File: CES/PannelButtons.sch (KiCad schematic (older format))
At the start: 16 parts

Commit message: Control Unit
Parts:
- gave numbers to parts that had none: 12
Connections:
- net BotEscM renamed BotMem
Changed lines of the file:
@@
 $Descr A4 11693 8268
 encoding utf-8
-Sheet 14 16
+Sheet 15 17
 Title ""
 Date ""
@@
 $EndDescr
 $Comp
-L Connector:Conn_01x08_Male J?
+L Connector:Conn_01x08_Male J1501
 U 1 1 61251A95
 P 700 6900
-F 0 "J?" H 800 6400 50  0000 C CNN
+F 0 "J1501" H 800 6400 50  0000 C CNN
 F 1 "PannelButtonsConnector" H 1200 7450 50  0000 C CNN
 F 2 "" H 700 6900 50  0001 C CNN
@@
 ~_IntPara
 $Comp
-L power:VCC #PWR?
+L power:VCC #PWR01501
 U 1 1 6085AA0D
 P 1450 900
-F 0 "#PWR?" H 1450 750 50  0001 C CNN
+F 0 "#PWR01501" H 1450 750 50  0001 C CNN
 F 1 "VCC" H 1465 1073 50  0000 C CNN
 F 2 "" H 1450 900 50  0001 C CNN
@@
 $EndComp
 $Comp
-L Device:R R?
+L Device:R R1501
 U 1 1 6085B8ED
 P 1450 1150
-F 0 "R?" H 1520 1196 50  0000 L CNN
+F 0 "R1501" H 1520 1196 50  0000 L CNN
 F 1 "1k5" H 1520 1105 50  0000 L CNN
 F 2 "" V 1380 1150 50  0001 C CNN
@@
 Connection ~ 1450 1450
 $Comp
-L 74xx:74HC00 U?
+L 74xx:74HC00 U1501
 U 1 1 6085C645
 P 7700 1050
-F 0 "U?" H 7700 1375 50  0000 C CNN
+F 0 "U1501" H 7700 1375 50  0000 C CNN
 F 1 "74HC00" H 7700 1284 50  0000 C CNN
 F 2 "" H 7700 1050 50  0001 C CNN
@@
 $EndComp
 $Comp
-L 74xx:74HC00 U?
+L 74xx:74HC00 U1501
 U 2 1 6085FDDA
 P 7700 1750
-F 0 "U?" H 7700 2075 50  0000 C CNN
+F 0 "U1501" H 7700 2075 50  0000 C CNN
 F 1 "74HC00" H 7700 1984 50  0000 C CNN
 F 2 "" H 7700 1750 50  0001 C CNN
@@
 $EndComp
 $Comp
-L 74xx:74HC00 U?
+L 74xx:74HC00 U1501
 U 3 1 60862050
 P 4250 1000
-F 0 "U?" H 4250 1325 50  0000 C CNN
+F 0 "U1501" H 4250 1325 50  0000 C CNN
 F 1 "74HC00" H 4250 1234 50  0000 C CNN
 F 2 "" H 4250 1000 50  0001 C CNN
@@
 $EndComp
 $Comp
-L 74xx:74HC00 U?
+L 74xx:74HC00 U1501
 U 4 1 60863680
 P 4250 1600
-F 0 "U?" H 4250 1925 50  0000 C CNN
+F 0 "U1501" H 4250 1925 50  0000 C CNN
 F 1 "74HC00" H 4250 1834 50  0000 C CNN
 F 2 "" H 4250 1600 50  0001 C CNN
@@
 $EndComp
 $Comp
-L 74xx:74HC00 U?
+L 74xx:74HC00 U1501
 U 5 1 608648EA
 P 3900 6750
-F 0 "U?" H 4130 6796 50  0000 L CNN
+F 0 "U1501" H 4130 6796 50  0000 L CNN
 F 1 "74HC00" H 4130 6705 50  0000 L CNN
 F 2 "" H 3900 6750 50  0001 C CNN
@@
 	5650 950  6750 950
 $Comp
-L Device:R R?
+L Device:R R1508
 U 1 1 6086CFA4
 P 6750 1450
-F 0 "R?" H 6820 1496 50  0000 L CNN
+F 0 "R1508" H 6820 1496 50  0000 L CNN
 F 1 "1k5" H 6820 1405 50  0000 L CNN
 F 2 "" V 6680 1450 50  0001 C CNN
@@
 $EndComp
 $Comp
-L Device:R R?
+L Device:R R1507
 U 1 1 6086D527
 P 6750 750
-F 0 "R?" H 6820 796 50  0000 L CNN
+F 0 "R1507" H 6820 796 50  0000 L CNN
 F 1 "1k5" H 6820 705 50  0000 L CNN
 F 2 "" V 6680 750 50  0001 C CNN
@@
 $EndComp
 $Comp
-L power:VCC #PWR?
+L power:VCC #PWR01511
 U 1 1 6086DE5E
 P 6750 500
-F 0 "#PWR?" H 6750 350 50  0001 C CNN
+F 0 "#PWR01511" H 6750 350 50  0001 C CNN
 F 1 "VCC" H 6765 673 50  0000 C CNN
 F 2 "" H 6750 500 50  0001 C CNN
@@
 $EndComp
 $Comp
-L power:VCC #PWR?
+L power:VCC #PWR01512
 U 1 1 6086E407
 P 6750 1200
-F 0 "#PWR?" H 6750 1050 50  0001 C CNN
+F 0 "#PWR01512" H 6750 1050 50  0001 C CNN
 F 1 "VCC" H 6765 1373 50  0000 C CNN
 F 2 "" H 6750 1200 50  0001 C CNN
@@
 P 9450 2050
 AR Path="/611BF25E/6087FD7D" Ref="U?"  Part="6"
-AR Path="/60832DB9/6125152F/6087FD7D" Ref="U?"  Part="6"
-F 0 "U?" H 9450 2367 50  0000 C CNN
+AR Path="/60832DB9/6125152F/6087FD7D" Ref="U1502"  Part="6"
+F 0 "U1502" H 9450 2367 50  0000 C CNN
 F 1 "74HC14" H 9450 2276 50  0000 C CNN
 F 2 "" H 9450 2050 50  0001 C CNN
@@
 _BotMudaP
 $Comp
-L power:VCC #PWR?
+L power:VCC #PWR01502
 U 1 1 60888B5F
 P 1450 1750
-F 0 "#PWR?" H 1450 1600 50  0001 C CNN
+F 0 "#PWR01502" H 1450 1600 50  0001 C CNN
 F 1 "VCC" H 1465 1923 50  0000 C CNN
 F 2 "" H 1450 1750 50  0001 C CNN
@@
 $EndComp
 $Comp
-L Device:R R?
+L Device:R R1502
 U 1 1 60888B65
 P 1450 2000
-F 0 "R?" H 1520 2046 50  0000 L CNN
+F 0 "R1502" H 1520 2046 50  0000 L CNN
 F 1 "1k5" H 1520 1955 50  0000 L CNN
 F 2 "" V 1380 2000 50  0001 C CNN
@@
 _BotMudaT
 $Comp
-L power:VCC #PWR?
+L power:VCC #PWR01503
 U 1 1 60891F96
 P 1450 2600
-F 0 "#PWR?" H 1450 2450 50  0001 C CNN
+F 0 "#PWR01503" H 1450 2450 50  0001 C CNN
 F 1 "VCC" H 1465 2773 50  0000 C CNN
 F 2 "" H 1450 2600 50  0001 C CNN
@@
 $EndComp
 $Comp
-L Device:R R?
+L Device:R R1503
 U 1 1 60891F9C
 P 1450 2850
-F 0 "R?" H 1520 2896 50  0000 L CNN
+F 0 "R1503" H 1520 2896 50  0000 L CNN
 F 1 "1k5" H 1520 2805 50  0000 L CNN
 F 2 "" V 1380 2850 50  0001 C CNN
@@
 _BotEscMem
 $Comp
-L power:VCC #PWR?
+L power:VCC #PWR01504
 U 1 1 60892ED6
 P 1450 3450
-F 0 "#PWR?" H 1450 3300 50  0001 C CNN
+F 0 "#PWR01504" H 1450 3300 50  0001 C CNN
 F 1 "VCC" H 1465 3623 50  0000 C CNN
 F 2 "" H 1450 3450 50  0001 C CNN
@@
 $EndComp
 $Comp
-L Device:R R?
+L Device:R R1504
 U 1 1 60892EDC
 P 1450 3700
-F 0 "R?" H 1520 3746 50  0000 L CNN
+F 0 "R1504" H 1520 3746 50  0000 L CNN
 F 1 "1k5" H 1520 3655 50  0000 L CNN
 F 2 "" V 1380 3700 50  0001 C CNN
@@
 	1450 3550 1450 3450
 Text GLabel 2100 4000 2    50   Output ~ 0
-BotEscM
+BotMem
 Wire Wire Line
 	1450 4000 2100 4000
@@
 _BotC1
 $Comp
-L power:VCC #PWR?
+L power:VCC #PWR01505
 U 1 1 60896662
 P 1450 4300
-F 0 "#PWR?" H 1450 4150 50  0001 C CNN
+F 0 "#PWR01505" H 1450 4150 50  0001 C CNN
 F 1 "VCC" H 1465 4473 50  0000 C CNN
 F 2 "" H 1450 4300 50  0001 C CNN
@@
 $EndComp
 $Comp
-L Device:R R?
+L Device:R R1505
 U 1 1 60896668
 P 1450 4550
-F 0 "R?" H 1520 4596 50  0000 L CNN
+F 0 "R1505" H 1520 4596 50  0000 L CNN
 F 1 "1k5" H 1520 4505 50  0000 L CNN
 F 2 "" V 1380 4550 50  0001 C CNN
@@
 _BotC0
 $Comp
-L power:VCC #PWR?
+L power:VCC #PWR01506
 U 1 1 60897AAE
 P 1450 5150
-F 0 "#PWR?" H 1450 5000 50  0001 C CNN
+F 0 "#PWR01506" H 1450 5000 50  0001 C CNN
 F 1 "VCC" H 1465 5323 50  0000 C CNN
 F 2 "" H 1450 5150 50  0001 C CNN
@@
 $EndComp
 $Comp
-L Device:R R?
+L Device:R R1506
 U 1 1 60897AB4
 P 1450 5400
-F 0 "R?" H 1520 5446 50  0000 L CNN
+F 0 "R1506" H 1520 5446 50  0000 L CNN
 F 1 "1k5" H 1520 5355 50  0000 L CNN
 F 2 "" V 1380 5400 50  0001 C CNN
@@
 Connection ~ 1450 5700
 $Comp
-L power:VCC #PWR?
+L power:VCC #PWR01507
 U 1 1 608AA437
 P 3900 6150
-F 0 "#PWR?" H 3900 6000 50  0001 C CNN
+F 0 "#PWR01507" H 3900 6000 50  0001 C CNN
 F 1 "VCC" H 3915 6323 50  0000 C CNN
 F 2 "" H 3900 6150 50  0001 C CNN
@@
 $EndComp
 $Comp
-L power:VCC #PWR?
+L power:VCC #PWR01509
 U 1 1 608AAE49
 P 5100 6550
-F 0 "#PWR?" H 5100 6400 50  0001 C CNN
+F 0 "#PWR01509" H 5100 6400 50  0001 C CNN
 F 1 "VCC" H 5115 6723 50  0000 C CNN
 F 2 "" H 5100 6550 50  0001 C CNN
@@
 $EndComp
 $Comp
-L power:GND #PWR?
+L power:GND #PWR01508
 U 1 1 608AB7C2
 P 3900 7350
-F 0 "#PWR?" H 3900 7100 50  0001 C CNN
+F 0 "#PWR01508" H 3900 7100 50  0001 C CNN
 F 1 "GND" H 3905 7177 50  0000 C CNN
 F 2 "" H 3900 7350 50  0001 C CNN
@@
 $EndComp
 $Comp
-L power:GND #PWR?
+L power:GND #PWR01510
 U 1 1 608ABC27
 P 5100 7050
-F 0 "#PWR?" H 5100 6800 50  0001 C CNN
+F 0 "#PWR01510" H 5100 6800 50  0001 C CNN
 F 1 "GND" H 5105 6877 50  0000 C CNN
 F 2 "" H 5100 7050 50  0001 C CNN
@@
 $EndComp
 $Comp
-L Device:C C?
+L Device:C C1501
 U 1 1 608AC627
 P 5100 6800
-F 0 "C?" H 5215 6846 50  0000 L CNN
+F 0 "C1501" H 5215 6846 50  0000 L CNN
 F 1 "100nF" H 5215 6755 50  0000 L CNN
 F 2 "" H 5138 6650 50  0001 C CNN

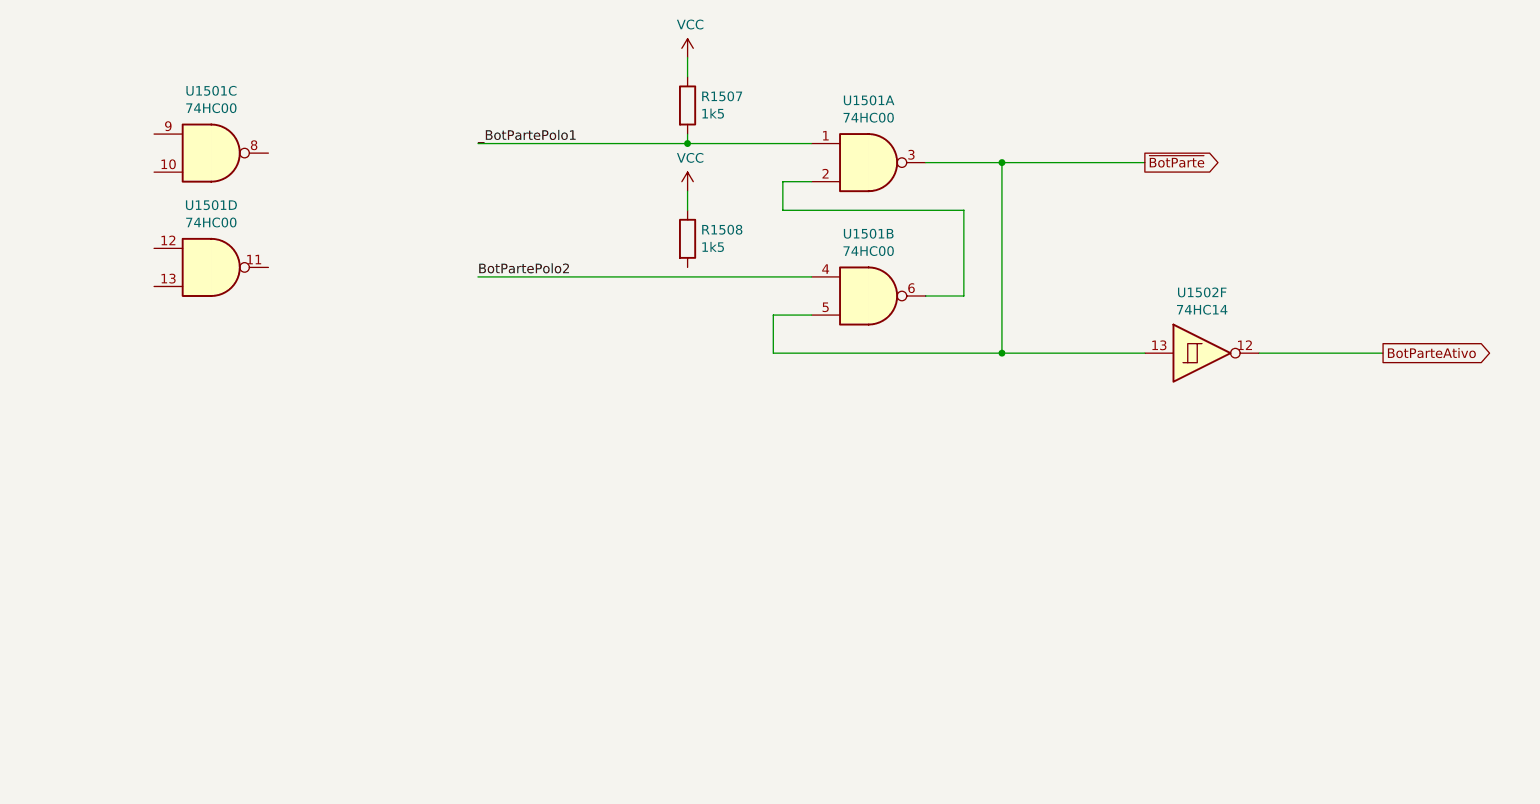
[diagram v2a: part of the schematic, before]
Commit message: Correcting ERC issues
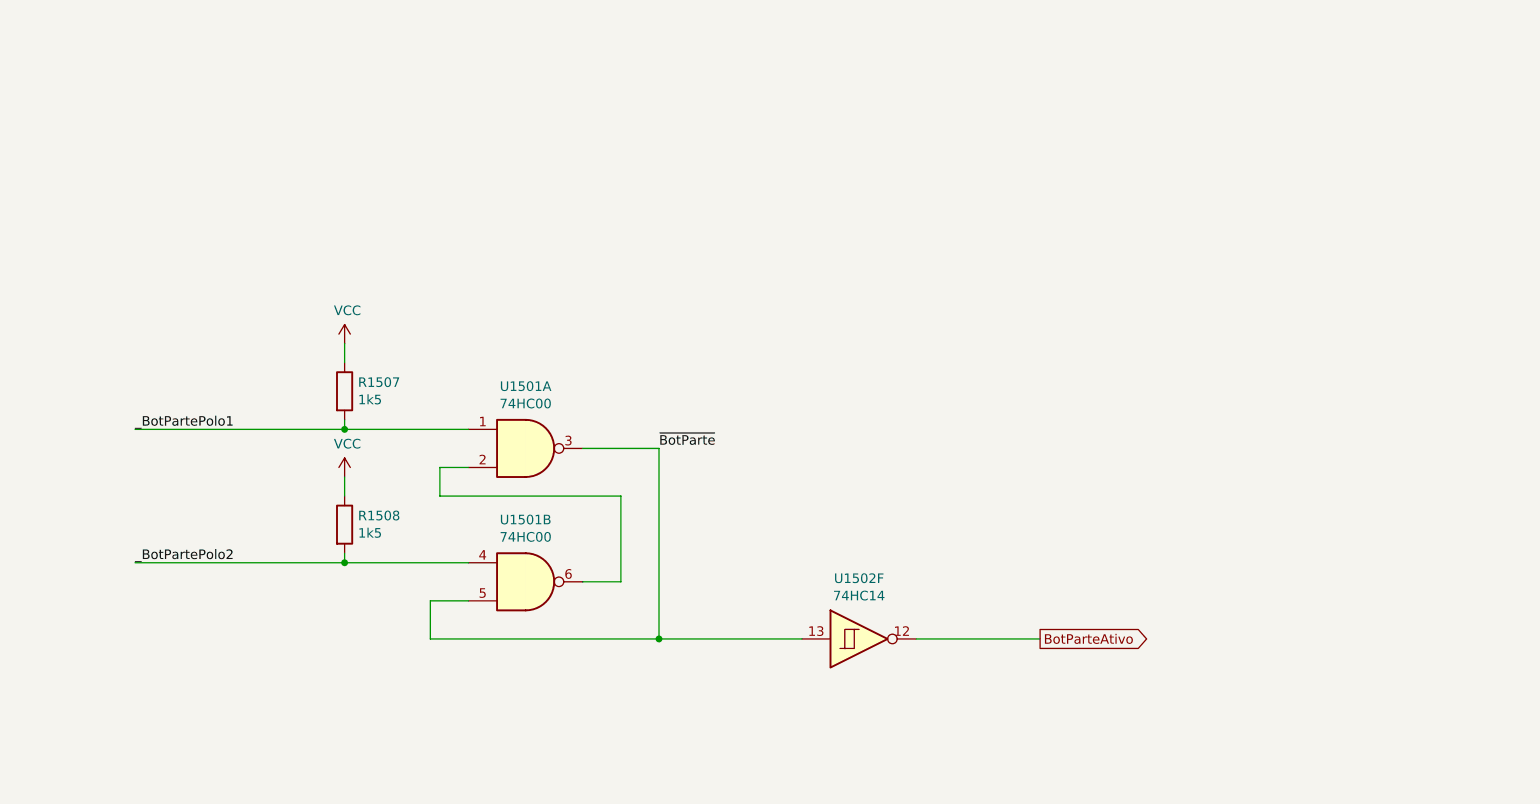
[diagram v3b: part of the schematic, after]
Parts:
- removed unit 3 of U1501
- removed unit 4 of U1501
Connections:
- net BotPartePolo2 is gone; now on net _BotPartePolo2: U1501.4
- net _BotPartePolo2: now also R1508.2
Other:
- moved on the sheet: R1507, R1508, U1501A, U1501B, U1502F
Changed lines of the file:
@@
 $Descr A4 11693 8268
 encoding utf-8
-Sheet 15 17
+Sheet 15 18
 Title ""
 Date ""
@@
 L 74xx:74HC00 U1501
 U 1 1 6085C645
-P 7700 1050
-F 0 "U1501" H 7700 1375 50  0000 C CNN
-F 1 "74HC00" H 7700 1284 50  0000 C CNN
-F 2 "" H 7700 1050 50  0001 C CNN
-F 3 "http://www.ti.com/lit/gpn/sn74hc00" H 7700 1050 50  0001 C CNN
-	1    7700 1050
+P 5900 2550
+F 0 "U1501" H 5900 2875 50  0000 C CNN
+F 1 "74HC00" H 5900 2784 50  0000 C CNN
+F 2 "" H 5900 2550 50  0001 C CNN
+F 3 "http://www.ti.com/lit/gpn/sn74hc00" H 5900 2550 50  0001 C CNN
+	1    5900 2550
 	1    0    0    -1
 $EndComp
@@
 L 74xx:74HC00 U1501
 U 2 1 6085FDDA
-P 7700 1750
-F 0 "U1501" H 7700 2075 50  0000 C CNN
-F 1 "74HC00" H 7700 1984 50  0000 C CNN
-F 2 "" H 7700 1750 50  0001 C CNN
-F 3 "http://www.ti.com/lit/gpn/sn74hc00" H 7700 1750 50  0001 C CNN
-	2    7700 1750
-	1    0    0    -1
-$EndComp
-$Comp
-L 74xx:74HC00 U1501
-U 3 1 60862050
-P 4250 1000
-F 0 "U1501" H 4250 1325 50  0000 C CNN
-F 1 "74HC00" H 4250 1234 50  0000 C CNN
-F 2 "" H 4250 1000 50  0001 C CNN
-F 3 "http://www.ti.com/lit/gpn/sn74hc00" H 4250 1000 50  0001 C CNN
-	3    4250 1000
-	1    0    0    -1
-$EndComp
-$Comp
-L 74xx:74HC00 U1501
-U 4 1 60863680
-P 4250 1600
-F 0 "U1501" H 4250 1925 50  0000 C CNN
-F 1 "74HC00" H 4250 1834 50  0000 C CNN
-F 2 "" H 4250 1600 50  0001 C CNN
-F 3 "http://www.ti.com/lit/gpn/sn74hc00" H 4250 1600 50  0001 C CNN
-	4    4250 1600
+P 5900 3250
+F 0 "U1501" H 5900 3575 50  0000 C CNN
+F 1 "74HC00" H 5900 3484 50  0000 C CNN
+F 2 "" H 5900 3250 50  0001 C CNN
+F 3 "http://www.ti.com/lit/gpn/sn74hc00" H 5900 3250 50  0001 C CNN
+	2    5900 3250
 	1    0    0    -1
 $EndComp
@@
 $EndComp
 Wire Wire Line
-	8000 1750 8200 1750
-Wire Wire Line
-	8200 1750 8200 1300
-Wire Wire Line
-	8200 1300 7250 1300
-Wire Wire Line
-	7250 1300 7250 1150
-Wire Wire Line
-	7250 1150 7400 1150
-Wire Wire Line
-	7400 1850 7200 1850
-Wire Wire Line
-	7200 1850 7200 2050
-Wire Wire Line
-	7200 2050 8400 2050
-Wire Wire Line
-	8400 2050 8400 1050
-Wire Wire Line
-	8400 1050 8000 1050
-Wire Wire Line
-	8400 1050 9150 1050
-Connection ~ 8400 1050
-Text GLabel 9150 1050 2    50   Output ~ 0
-~BotParte
-Text Label 5650 950  0    50   ~ 0
+	6200 3250 6400 3250
+Wire Wire Line
+	6400 3250 6400 2800
+Wire Wire Line
+	6400 2800 5450 2800
+Wire Wire Line
+	5450 2800 5450 2650
+Wire Wire Line
+	5450 2650 5600 2650
+Wire Wire Line
+	5600 3350 5400 3350
+Wire Wire Line
+	5400 3350 5400 3550
+Wire Wire Line
+	5400 3550 6600 3550
+Wire Wire Line
+	6600 3550 6600 2550
+Wire Wire Line
+	6600 2550 6200 2550
+Text Label 3850 2450 0    50   ~ 0
 _BotPartePolo1
-Text Label 5650 1650 0    50   ~ 0
-BotPartePolo2
-Wire Wire Line
-	5650 1650 7400 1650
-Wire Wire Line
-	5650 950  6750 950
+Text Label 3850 3150 0    50   ~ 0
+_BotPartePolo2
+Wire Wire Line
+	3850 3150 4950 3150
+Wire Wire Line
+	3850 2450 4950 2450
 $Comp
 L Device:R R1508
 U 1 1 6086CFA4
-P 6750 1450
-F 0 "R1508" H 6820 1496 50  0000 L CNN
-F 1 "1k5" H 6820 1405 50  0000 L CNN
-F 2 "" V 6680 1450 50  0001 C CNN
-F 3 "~" H 6750 1450 50  0001 C CNN
-	1    6750 1450
+P 4950 2950
+F 0 "R1508" H 5020 2996 50  0000 L CNN
+F 1 "1k5" H 5020 2905 50  0000 L CNN
+F 2 "" V 4880 2950 50  0001 C CNN
+F 3 "~" H 4950 2950 50  0001 C CNN
+	1    4950 2950
 	1    0    0    -1
 $EndComp
@@
 L Device:R R1507
 U 1 1 6086D527
-P 6750 750
-F 0 "R1507" H 6820 796 50  0000 L CNN
-F 1 "1k5" H 6820 705 50  0000 L CNN
-F 2 "" V 6680 750 50  0001 C CNN
-F 3 "~" H 6750 750 50  0001 C CNN
-	1    6750 750
+P 4950 2250
+F 0 "R1507" H 5020 2296 50  0000 L CNN
+F 1 "1k5" H 5020 2205 50  0000 L CNN
+F 2 "" V 4880 2250 50  0001 C CNN
+F 3 "~" H 4950 2250 50  0001 C CNN
+	1    4950 2250
 	1    0    0    -1
 $EndComp
@@
 L power:VCC #PWR01511
 U 1 1 6086DE5E
-P 6750 500
-F 0 "#PWR01511" H 6750 350 50  0001 C CNN
-F 1 "VCC" H 6765 673 50  0000 C CNN
-F 2 "" H 6750 500 50  0001 C CNN
-F 3 "" H 6750 500 50  0001 C CNN
-	1    6750 500
+P 4950 2000
+F 0 "#PWR01511" H 4950 1850 50  0001 C CNN
+F 1 "VCC" H 4965 2173 50  0000 C CNN
+F 2 "" H 4950 2000 50  0001 C CNN
+F 3 "" H 4950 2000 50  0001 C CNN
+	1    4950 2000
 	1    0    0    -1
 $EndComp
@@
 L power:VCC #PWR01512
 U 1 1 6086E407
-P 6750 1200
-F 0 "#PWR01512" H 6750 1050 50  0001 C CNN
-F 1 "VCC" H 6765 1373 50  0000 C CNN
-F 2 "" H 6750 1200 50  0001 C CNN
-F 3 "" H 6750 1200 50  0001 C CNN
-	1    6750 1200
-	1    0    0    -1
-$EndComp
-Wire Wire Line
-	6750 1200 6750 1300
-Wire Wire Line
-	6750 900  6750 950
-Connection ~ 6750 950
-Wire Wire Line
-	6750 950  7400 950
-Wire Wire Line
-	6750 500  6750 600
+P 4950 2700
+F 0 "#PWR01512" H 4950 2550 50  0001 C CNN
+F 1 "VCC" H 4965 2873 50  0000 C CNN
+F 2 "" H 4950 2700 50  0001 C CNN
+F 3 "" H 4950 2700 50  0001 C CNN
+	1    4950 2700
+	1    0    0    -1
+$EndComp
+Wire Wire Line
+	4950 2700 4950 2800
+Wire Wire Line
+	4950 2400 4950 2450
+Connection ~ 4950 2450
+Wire Wire Line
+	4950 2450 5600 2450
+Wire Wire Line
+	4950 2000 4950 2100
 $Comp
 L 74xx:74HC14 U?
 U 6 1 6087FD7D
-P 9450 2050
+P 7650 3550
 AR Path="/611BF25E/6087FD7D" Ref="U?"  Part="6"
 AR Path="/60832DB9/6125152F/6087FD7D" Ref="U1502"  Part="6"
-F 0 "U1502" H 9450 2367 50  0000 C CNN
-F 1 "74HC14" H 9450 2276 50  0000 C CNN
-F 2 "" H 9450 2050 50  0001 C CNN
-F 3 "http://www.ti.com/lit/gpn/sn74HC14" H 9450 2050 50  0001 C CNN
-	6    9450 2050
-	1    0    0    -1
-$EndComp
-Wire Wire Line
-	8400 2050 9150 2050
-Connection ~ 8400 2050
-Text GLabel 10400 2050 2    50   Output ~ 0
+F 0 "U1502" H 7650 3867 50  0000 C CNN
+F 1 "74HC14" H 7650 3776 50  0000 C CNN
+F 2 "" H 7650 3550 50  0001 C CNN
+F 3 "http://www.ti.com/lit/gpn/sn74HC14" H 7650 3550 50  0001 C CNN
+	6    7650 3550
+	1    0    0    -1
+$EndComp
+Wire Wire Line
+	6600 3550 7350 3550
+Connection ~ 6600 3550
+Text GLabel 8600 3550 2    50   Output ~ 0
 BotParteAtivo
 Wire Wire Line
-	10400 2050 9750 2050
+	8600 3550 7950 3550
 Text Label 900  2300 0    50   ~ 0
 _BotMudaP
@@
 Wire Wire Line
 	3900 6250 3900 6150
+Wire Wire Line
+	4950 3100 4950 3150
+Connection ~ 4950 3150
+Wire Wire Line
+	4950 3150 5600 3150
+Text Label 6600 2550 0    50   ~ 0
+~BotParte
 $EndSCHEMATC

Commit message: Assigning footprints and generating netlist
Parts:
- C1501: footprint (none) -> Capacitor_THT:CP_Radial_D5.0mm_P2.50mm
- J1501: footprint (none) -> Connector_PinHeader_2.54mm:PinHeader_1x08_P2.54mm_Vertical
- R1501, R1502, R1503, R1504, R1505, R1506, R1507, R1508: footprint (none) -> Resistor_THT:R_Axial_DIN0204_L3.6mm_D1.6mm_P1.90mm_Vertical
- U1501, U1502: footprint (none) -> Package_DIP:DIP-14_W7.62mm
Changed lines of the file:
@@
 F 0 "J1501" H 800 6400 50  0000 C CNN
 F 1 "PannelButtonsConnector" H 1200 7450 50  0000 C CNN
-F 2 "" H 700 6900 50  0001 C CNN
+F 2 "Connector_PinHeader_2.54mm:PinHeader_1x08_P2.54mm_Vertical" H 700 6900 50  0001 C CNN
 F 3 "~" H 700 6900 50  0001 C CNN
 	1    700  6900
@@
 F 0 "R1501" H 1520 1196 50  0000 L CNN
 F 1 "1k5" H 1520 1105 50  0000 L CNN
-F 2 "" V 1380 1150 50  0001 C CNN
+F 2 "Resistor_THT:R_Axial_DIN0204_L3.6mm_D1.6mm_P1.90mm_Vertical" V 1380 1150 50  0001 C CNN
 F 3 "~" H 1450 1150 50  0001 C CNN
 	1    1450 1150
@@
 F 0 "U1501" H 5900 2875 50  0000 C CNN
 F 1 "74HC00" H 5900 2784 50  0000 C CNN
-F 2 "" H 5900 2550 50  0001 C CNN
+F 2 "Package_DIP:DIP-14_W7.62mm" H 5900 2550 50  0001 C CNN
 F 3 "http://www.ti.com/lit/gpn/sn74hc00" H 5900 2550 50  0001 C CNN
 	1    5900 2550
@@
 F 0 "U1501" H 5900 3575 50  0000 C CNN
 F 1 "74HC00" H 5900 3484 50  0000 C CNN
-F 2 "" H 5900 3250 50  0001 C CNN
+F 2 "Package_DIP:DIP-14_W7.62mm" H 5900 3250 50  0001 C CNN
 F 3 "http://www.ti.com/lit/gpn/sn74hc00" H 5900 3250 50  0001 C CNN
 	2    5900 3250
@@
 F 0 "U1501" H 4130 6796 50  0000 L CNN
 F 1 "74HC00" H 4130 6705 50  0000 L CNN
-F 2 "" H 3900 6750 50  0001 C CNN
+F 2 "Package_DIP:DIP-14_W7.62mm" H 3900 6750 50  0001 C CNN
 F 3 "http://www.ti.com/lit/gpn/sn74hc00" H 3900 6750 50  0001 C CNN
 	5    3900 6750
@@
 F 0 "R1508" H 5020 2996 50  0000 L CNN
 F 1 "1k5" H 5020 2905 50  0000 L CNN
-F 2 "" V 4880 2950 50  0001 C CNN
+F 2 "Resistor_THT:R_Axial_DIN0204_L3.6mm_D1.6mm_P1.90mm_Vertical" V 4880 2950 50  0001 C CNN
 F 3 "~" H 4950 2950 50  0001 C CNN
 	1    4950 2950
@@
 F 0 "R1507" H 5020 2296 50  0000 L CNN
 F 1 "1k5" H 5020 2205 50  0000 L CNN
-F 2 "" V 4880 2250 50  0001 C CNN
+F 2 "Resistor_THT:R_Axial_DIN0204_L3.6mm_D1.6mm_P1.90mm_Vertical" V 4880 2250 50  0001 C CNN
 F 3 "~" H 4950 2250 50  0001 C CNN
 	1    4950 2250
@@
 F 0 "U1502" H 7650 3867 50  0000 C CNN
 F 1 "74HC14" H 7650 3776 50  0000 C CNN
-F 2 "" H 7650 3550 50  0001 C CNN
+F 2 "Package_DIP:DIP-14_W7.62mm" H 7650 3550 50  0001 C CNN
 F 3 "http://www.ti.com/lit/gpn/sn74HC14" H 7650 3550 50  0001 C CNN
 	6    7650 3550
@@
 F 0 "R1502" H 1520 2046 50  0000 L CNN
 F 1 "1k5" H 1520 1955 50  0000 L CNN
-F 2 "" V 1380 2000 50  0001 C CNN
+F 2 "Resistor_THT:R_Axial_DIN0204_L3.6mm_D1.6mm_P1.90mm_Vertical" V 1380 2000 50  0001 C CNN
 F 3 "~" H 1450 2000 50  0001 C CNN
 	1    1450 2000
@@
 F 0 "R1503" H 1520 2896 50  0000 L CNN
 F 1 "1k5" H 1520 2805 50  0000 L CNN
-F 2 "" V 1380 2850 50  0001 C CNN
+F 2 "Resistor_THT:R_Axial_DIN0204_L3.6mm_D1.6mm_P1.90mm_Vertical" V 1380 2850 50  0001 C CNN
 F 3 "~" H 1450 2850 50  0001 C CNN
 	1    1450 2850
@@
 F 0 "R1504" H 1520 3746 50  0000 L CNN
 F 1 "1k5" H 1520 3655 50  0000 L CNN
-F 2 "" V 1380 3700 50  0001 C CNN
+F 2 "Resistor_THT:R_Axial_DIN0204_L3.6mm_D1.6mm_P1.90mm_Vertical" V 1380 3700 50  0001 C CNN
 F 3 "~" H 1450 3700 50  0001 C CNN
 	1    1450 3700
@@
 F 0 "R1505" H 1520 4596 50  0000 L CNN
 F 1 "1k5" H 1520 4505 50  0000 L CNN
-F 2 "" V 1380 4550 50  0001 C CNN
+F 2 "Resistor_THT:R_Axial_DIN0204_L3.6mm_D1.6mm_P1.90mm_Vertical" V 1380 4550 50  0001 C CNN
 F 3 "~" H 1450 4550 50  0001 C CNN
 	1    1450 4550
@@
 F 0 "R1506" H 1520 5446 50  0000 L CNN
 F 1 "1k5" H 1520 5355 50  0000 L CNN
-F 2 "" V 1380 5400 50  0001 C CNN
+F 2 "Resistor_THT:R_Axial_DIN0204_L3.6mm_D1.6mm_P1.90mm_Vertical" V 1380 5400 50  0001 C CNN
 F 3 "~" H 1450 5400 50  0001 C CNN
 	1    1450 5400
@@
 F 0 "C1501" H 5215 6846 50  0000 L CNN
 F 1 "100nF" H 5215 6755 50  0000 L CNN
-F 2 "" H 5138 6650 50  0001 C CNN
+F 2 "Capacitor_THT:CP_Radial_D5.0mm_P2.50mm" H 5138 6650 50  0001 C CNN
 F 3 "~" H 5100 6800 50  0001 C CNN
 	1    5100 6800
